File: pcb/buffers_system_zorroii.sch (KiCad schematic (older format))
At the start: 38 parts

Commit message: FPGA side labels added
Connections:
- net _FPGA_DSACK1: now reaches X?.1 (A)
- net _FPGA_DSACK0: now reaches X?.1 (A)
- net _FPGA_BERR: now reaches X?.2 (B)
- net FPGA_CPUCLK_A: now reaches X?.2 (B)
- net _FPGA_HLT: now reaches X?.2 (B)
- net _FPGA_IPL2: now reaches X?.2 (B)
- net _FPGA_IPL1: now reaches X?.2 (B)
- net _FPGA_IPL0: now reaches X?.2 (B)
- net _FPGA_RST: now reaches X?.2 (B)
- net _FPGA_KB_RESET: now reaches X?.2 (B)
- net A_BUFF_OE renamed _A_BUFF_OE
- net INONLY_BUFF_OE renamed _INONLY_BUFF_OE
- net _CPUCLK_A renamed CPUCLK_A
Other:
- moved on the sheet: X?
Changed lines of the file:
@@
 FPGA
 Entry Wire Line
-	2000 1450 2100 1550
-Entry Wire Line
-	2000 1550 2100 1650
+	1900 1450 2000 1550
+Entry Wire Line
+	1900 1550 2000 1650
 Entry Wire Line
 	1400 4000 1500 4100
@@
 L WM1200:testpoint_cutline X?
 U 1 1 5E6A95DB
-P 2800 1600
-F 0 "X?" H 2800 1650 50  0000 C CNN
-F 1 "testpoint_cutline" H 2800 1750 50  0001 C CNN
-F 2 "" H 2950 1600 50  0001 C CNN
-F 3 "" H 2950 1600 50  0001 C CNN
-	1    2800 1600
-	1    0    0    -1
-$EndComp
-Wire Wire Line
-	2100 1550 2400 1550
+P 3050 1600
+F 0 "X?" H 3050 1650 50  0000 C CNN
+F 1 "testpoint_cutline" H 3050 1750 50  0001 C CNN
+F 2 "" H 3200 1600 50  0001 C CNN
+F 3 "" H 3200 1600 50  0001 C CNN
+	1    3050 1600
+	1    0    0    -1
+$EndComp
+Wire Wire Line
+	2000 1550 2650 1550
 $Comp
 L WM1200:testpoint_cutline X?
@@
 $EndComp
 Wire Wire Line
-	3200 1550 3500 1550
-Wire Wire Line
-	3500 1650 3200 1650
+	3450 1550 3500 1550
+Wire Wire Line
+	3500 1650 3450 1650
 Wire Wire Line
 	1850 3200 2400 3200
@@
 _BERR
 Text Label 1900 3300 0    50   ~ 0
-_CPUCLK_A
+CPUCLK_A
 Text Label 1900 3400 0    50   ~ 0
 _HLT
@@
 	7050 5600 6250 5600
 Text Label 6400 5600 0    50   ~ 0
-INONLY_BUFF_OE
+_INONLY_BUFF_OE
 Text Label 5600 5600 0    50   ~ 0
 GND
@@
 L WM1200:testpoint_cutline X?
 U 1 1 5E6AA8F6
-P 2800 1700
-F 0 "X?" H 2800 1750 50  0000 C CNN
-F 1 "testpoint_cutline" H 2800 1850 50  0001 C CNN
-F 2 "" H 2950 1700 50  0001 C CNN
-F 3 "" H 2950 1700 50  0001 C CNN
-	1    2800 1700
-	1    0    0    -1
-$EndComp
-Wire Wire Line
-	2100 1650 2400 1650
-Wire Bus Line
-	2000 2950 7150 2950
+P 3050 1700
+F 0 "X?" H 3050 1750 50  0000 C CNN
+F 1 "testpoint_cutline" H 3050 1850 50  0001 C CNN
+F 2 "" H 3200 1700 50  0001 C CNN
+F 3 "" H 3200 1700 50  0001 C CNN
+	1    3050 1700
+	1    0    0    -1
+$EndComp
+Wire Wire Line
+	2000 1650 2650 1650
+Wire Bus Line
+	1900 2950 7150 2950
 Connection ~ 7150 2950
 Text Notes 3450 1350 0    50   ~ 0
@@
 L WM1200:testpoint X?
 U 1 1 5E96DC89
-P 2950 1700
-F 0 "X?" H 3000 1750 50  0000 C CNN
-F 1 "testpoint" H 2950 1850 50  0001 C CNN
-F 2 "" H 2950 1700 50  0001 C CNN
-F 3 "" H 2950 1700 50  0001 C CNN
-	1    2950 1700
+P 3200 1700
+F 0 "X?" H 3250 1750 50  0000 C CNN
+F 1 "testpoint" H 3200 1850 50  0001 C CNN
+F 2 "" H 3200 1700 50  0001 C CNN
+F 3 "" H 3200 1700 50  0001 C CNN
+	1    3200 1700
 	-1   0    0    1
 $EndComp
@@
 L WM1200:testpoint X?
 U 1 1 5E97030F
-P 2950 1800
-F 0 "X?" H 3000 1850 50  0000 C CNN
-F 1 "testpoint" H 2950 1950 50  0001 C CNN
-F 2 "" H 2950 1800 50  0001 C CNN
-F 3 "" H 2950 1800 50  0001 C CNN
-	1    2950 1800
+P 3200 1800
+F 0 "X?" H 3250 1850 50  0000 C CNN
+F 1 "testpoint" H 3200 1950 50  0001 C CNN
+F 2 "" H 3200 1800 50  0001 C CNN
+F 3 "" H 3200 1800 50  0001 C CNN
+	1    3200 1800
 	-1   0    0    1
 $EndComp
@@
 L WM1200:testpoint X?
 U 1 1 5E972706
-P 2950 1900
-F 0 "X?" H 3000 1950 50  0000 C CNN
-F 1 "testpoint" H 2950 2050 50  0001 C CNN
-F 2 "" H 2950 1900 50  0001 C CNN
-F 3 "" H 2950 1900 50  0001 C CNN
-	1    2950 1900
+P 3200 1900
+F 0 "X?" H 3250 1950 50  0000 C CNN
+F 1 "testpoint" H 3200 2050 50  0001 C CNN
+F 2 "" H 3200 1900 50  0001 C CNN
+F 3 "" H 3200 1900 50  0001 C CNN
+	1    3200 1900
 	-1   0    0    1
 $EndComp
@@
 L WM1200:testpoint X?
 U 1 1 5E974A69
-P 2950 2000
-F 0 "X?" H 3000 2050 50  0000 C CNN
-F 1 "testpoint" H 2950 2150 50  0001 C CNN
-F 2 "" H 2950 2000 50  0001 C CNN
-F 3 "" H 2950 2000 50  0001 C CNN
-	1    2950 2000
+P 3200 2000
+F 0 "X?" H 3250 2050 50  0000 C CNN
+F 1 "testpoint" H 3200 2150 50  0001 C CNN
+F 2 "" H 3200 2000 50  0001 C CNN
+F 3 "" H 3200 2000 50  0001 C CNN
+	1    3200 2000
 	-1   0    0    1
 $EndComp
@@
 L WM1200:testpoint X?
 U 1 1 5E976D83
-P 2950 2100
-F 0 "X?" H 3000 2150 50  0000 C CNN
-F 1 "testpoint" H 2950 2250 50  0001 C CNN
-F 2 "" H 2950 2100 50  0001 C CNN
-F 3 "" H 2950 2100 50  0001 C CNN
-	1    2950 2100
+P 3200 2100
+F 0 "X?" H 3250 2150 50  0000 C CNN
+F 1 "testpoint" H 3200 2250 50  0001 C CNN
+F 2 "" H 3200 2100 50  0001 C CNN
+F 3 "" H 3200 2100 50  0001 C CNN
+	1    3200 2100
 	-1   0    0    1
 $EndComp
@@
 L WM1200:testpoint X?
 U 1 1 5E979098
-P 2950 2200
-F 0 "X?" H 3000 2250 50  0000 C CNN
-F 1 "testpoint" H 2950 2350 50  0001 C CNN
-F 2 "" H 2950 2200 50  0001 C CNN
-F 3 "" H 2950 2200 50  0001 C CNN
-	1    2950 2200
+P 3200 2200
+F 0 "X?" H 3250 2250 50  0000 C CNN
+F 1 "testpoint" H 3200 2350 50  0001 C CNN
+F 2 "" H 3200 2200 50  0001 C CNN
+F 3 "" H 3200 2200 50  0001 C CNN
+	1    3200 2200
 	-1   0    0    1
 $EndComp
@@
 $EndComp
 Wire Wire Line
-	3200 1750 3500 1750
-Wire Wire Line
-	3500 1850 3200 1850
-Wire Wire Line
-	3200 1950 3500 1950
-Wire Wire Line
-	3500 2050 3200 2050
-Wire Wire Line
-	3200 2150 3500 2150
-Wire Wire Line
-	3500 2250 3200 2250
+	3450 1750 3500 1750
+Wire Wire Line
+	3500 1850 3450 1850
+Wire Wire Line
+	3450 1950 3500 1950
+Wire Wire Line
+	3500 2050 3450 2050
+Wire Wire Line
+	3450 2150 3500 2150
+Wire Wire Line
+	3500 2250 3450 2250
 Wire Wire Line
 	5150 1550 4800 1550
@@
 	6700 1650 5950 1650
 Text Label 6100 2550 0    50   ~ 0
-A_BUFF_OE
+_A_BUFF_OE
 Text Label 6100 2650 0    50   ~ 0
 A_BUFF_DIR
@@
 	7050 3900 5900 3900
 Text Label 5050 4100 0    50   ~ 0
-INONLY_BUFF_OE
+_INONLY_BUFF_OE
 Text Label 5050 4200 0    50   ~ 0
 INONLY_BUFF_DIR
@@
 +3V3_BUFFER
 Wire Bus Line
+	1400 5800 5500 5800
+Text Label 2000 1550 0    50   ~ 0
+_FPGA_DSACK1
+Text Label 2000 1650 0    50   ~ 0
+_FPGA_DSACK0
+Wire Bus Line
 	7150 2650 7150 2950
 Wire Bus Line
-	2000 1450 2000 2950
+	1900 1450 1900 2950
 Wire Bus Line
 	6800 1200 6800 1750
@@
 Wire Bus Line
 	7150 2950 7150 6300
-Wire Bus Line
-	1400 5800 5500 5800
+Text Label 6250 3200 0    50   ~ 0
+_FPGA_BERR
+Text Label 6250 3300 0    50   ~ 0
+FPGA_CPUCLK_A
+Text Label 6250 3400 0    50   ~ 0
+_FPGA_HLT
+Text Label 6250 3500 0    50   ~ 0
+_FPGA_IPL2
+Text Label 6250 3600 0    50   ~ 0
+_FPGA_IPL1
+Text Label 6250 3700 0    50   ~ 0
+_FPGA_IPL0
+Text Label 6250 3800 0    50   ~ 0
+_FPGA_RST
+Text Label 6250 3900 0    50   ~ 0
+_FPGA_KB_RESET
 $EndSCHEMATC

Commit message: Some work done on the whole project
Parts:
- removed D? (x2): 74LVCH162245A, symbol WM1200:74LVCH162245A
- added U5: 74LVCH162245A, symbol WM1200:74LVCH162245A
- added XT54, XT55: testpoint_cutline, symbol WM1200:testpoint_cutline
- gave numbers to parts that had none: 36
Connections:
- net +3V3_BUFFER: now also U5.18 (VCC), U5.31 (VCC), U5.42 (VCC), U5.7 (VCC)
- net A_BUFF_DIR: now also U5.1 (1DIR)
- net GND: now also U5.10 (GND), U5.15 (GND), U5.21 (GND), U5.28 (GND), U5.34 (GND), U5.39 (GND), U5.4 (GND), U5.45 (GND)
- net INONLY_BUFF_DIR: now also U5.24 (2DIR), XT55.1 (A)
- net _A_BUFF_OE: now also U5.48 (_1OE)
- net _INONLY_BUFF_OE: now also U5.25 (_2OE), XT54.1 (A)
- net at XT36.1 (tp): now also U5.11 (1B6)
- net at XT37.1 (tp): now also U5.12 (1B7)
- net at XT30.2 (B): now also U5.2 (1B0)
- net at XT31.2 (B): now also U5.3 (1B1)
- net at XT43.1 (tp): now also U5.37 (1A7)
- net at XT42.1 (tp): now also U5.38 (1A6)
- net at XT41.1 (tp): now also U5.40 (1A5)
- net at XT40.1 (tp): now also U5.41 (1A4)
- net at XT39.1 (tp): now also U5.43 (1A3)
- net at XT38.1 (tp): now also U5.44 (1A2)
- net at XT53.1 (A): now also U5.46 (1A1)
- net at XT52.1 (A): now also U5.47 (1A0)
- net at XT32.1 (tp): now also U5.5 (1B2)
- net at XT33.1 (tp): now also U5.6 (1B3)
- net at XT34.1 (tp): now also U5.8 (1B4)
- net at XT35.1 (tp): now also U5.9 (1B5)
- net at XT22.2 (B): now also U5.13 (2B0)
- net at XT23.2 (B): now also U5.14 (2B1)
- net at XT24.2 (B): now also U5.16 (2B2)
- net at XT25.2 (B): now also U5.17 (2B3)
- net at XT26.2 (B): now also U5.19 (2B4)
- net at XT27.2 (B): now also U5.20 (2B5)
- net at XT28.2 (B): now also U5.22 (2B6)
- net at XT29.2 (B): now also U5.23 (2B7)
- net at XT51.1 (A): now also U5.26 (2A7)
- net at XT50.1 (A): now also U5.27 (2A6)
- net at XT49.1 (A): now also U5.29 (2A5)
- net at XT48.1 (A): now also U5.30 (2A4)
- net at XT47.1 (A): now also U5.32 (2A3)
- net at XT46.1 (A): now also U5.33 (2A2)
- net at XT45.1 (A): now also U5.35 (2A1)
- net at XT44.1 (A): now also U5.36 (2A0)

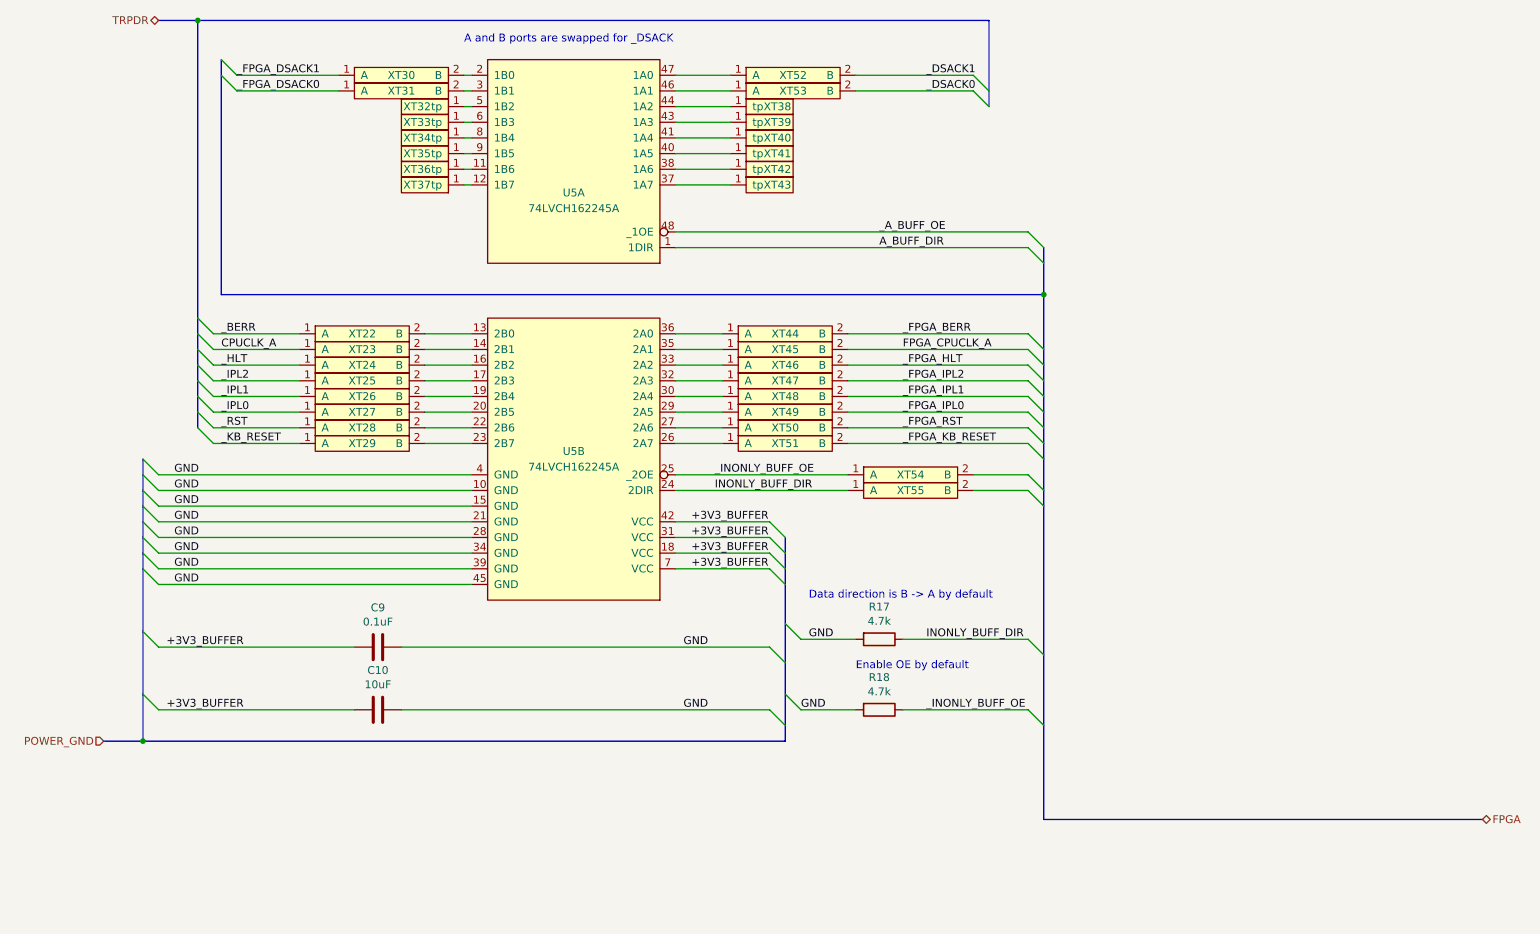
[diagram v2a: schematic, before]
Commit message: ok, we are using global labels now
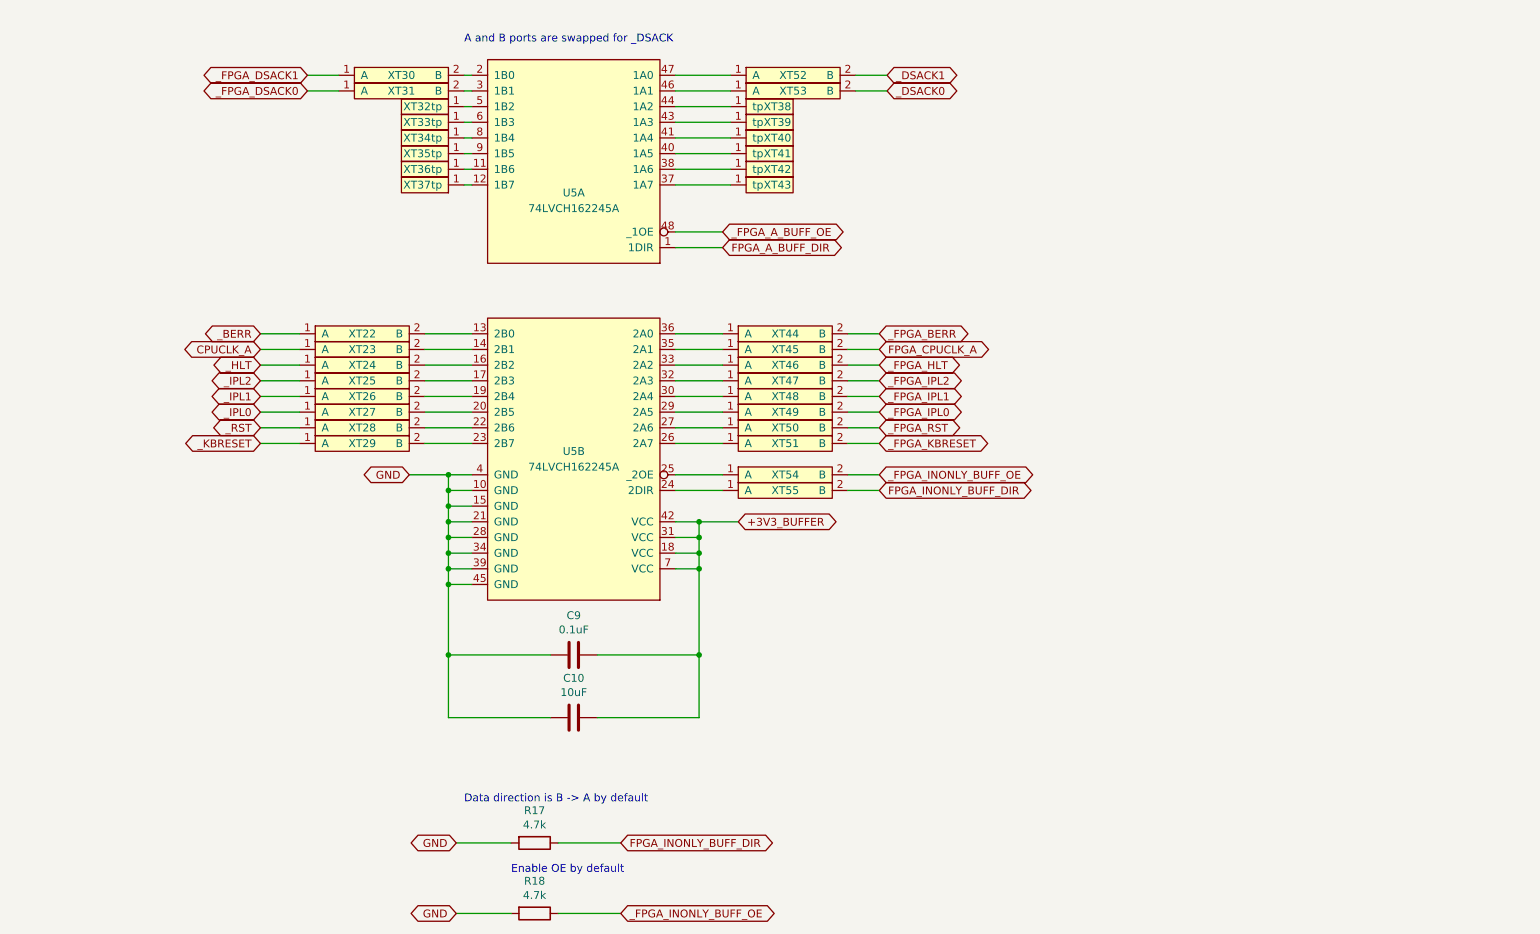
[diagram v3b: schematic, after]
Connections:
- net +3V3_BUFFER: now also C10.2, C9.2; no longer C10.1, C9.1
- net GND: now also C10.1, C9.1; no longer C10.2, C9.2
- net _FPGA_INONLY_BUFF_OE: now reaches XT54.2 (B)
- net _FPGA_INONLY_BUFF_OE: now also R18.1
- net FPGA_INONLY_BUFF_DIR: now reaches XT55.2 (B)
- net FPGA_INONLY_BUFF_DIR: now also R17.1
- net A_BUFF_DIR renamed FPGA_A_BUFF_DIR
- net INONLY_BUFF_DIR: no longer names the net of U5.24 (2DIR), XT55.1 (A)
- net INONLY_BUFF_DIR: no longer R17.1
- net _A_BUFF_OE renamed _FPGA_A_BUFF_OE
- net _FPGA_KB_RESET renamed _FPGA_KBRESET
- net _INONLY_BUFF_OE: no longer names the net of U5.25 (_2OE), XT54.1 (A)
- net _INONLY_BUFF_OE: no longer R18.1
- net _KB_RESET renamed _KBRESET
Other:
- moved on the sheet: C10, C9, R17, R18, XT54, XT55
